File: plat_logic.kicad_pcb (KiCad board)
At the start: 2 copper layers, 100 x 100 mm, 135 parts, among them CN1 GPS_Port, Con2 DS1023-1X2SF11, J1 USB_C_Receptacle, J10 DS1023-1X8SF11, J11 DS1023-1X5SF11, J12 DS1023-1X5SF11, J13 DS1023-1X5SF11, J14 DS1023-1X5SF11, J15 DS1023-1X5SF11, J16 DS1023-1X5SF11, J17 DS1023-1X5SF11, J2 JST_GH_SM06B-GHS-TB, J3 JST_GH_SM06B-GHS-TB, J4 JST_GH_SM06B-GHS-TB, J5 JST_GH_SM06B-GHS-TB, J6 DS1023-1X11S21, J7 DS1023-1X11S21, J8 DS1023-1X6SF11, J9 DS1023-1X11S21, SW1 Button-SMD-4.5x4.5x5.5, SW2 Button-SMD-4.5x4.5x5.5, U1 STM32F429ZITx, U2 USBLC6-2SC6, U3 SN65HVD232, Y1 CSTNE8M00GH5L000R0 8.000MHZ, Y2 NX3215SA-32.768KHZ-EXS00A-MU0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, con1 DS1023-1X3SF11

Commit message: trassing
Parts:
- moved C6 16.5 mm to (127.6, 114.5), turned to 45 degrees
- moved C7 16.3 mm to (129.3, 116.2), turned to -135 degrees
- moved C8 16.3 mm to (130.8, 117.7)
- moved R14 16.3 mm to (131.4, 113.8)
- moved R13 16.3 mm to (130.0, 112.4)
- moved R15 16.2 mm to (132.9, 115.2)
- moved C12 7.85 mm to (134.2, 117.5), turned to 135 degrees
- moved R6 6.45 mm to (167.7, 114.2), turned to -45 degrees
- moved R5 5.99 mm to (165.0, 116.7), turned to -45 degrees
- moved C9 5.40 mm to (168.4, 100.1), turned to 45 degrees
- moved R18 4.74 mm to (168.6, 102.4), turned to -135 degrees
- moved R3 3.25 mm to (166.4, 115.3)
- moved C24 2.55 mm to (161.4, 118.9)
- moved C27 2.54 mm to (158.5, 121.8)
- moved C29 2.49 mm to (156.8, 123.4)
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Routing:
- net GND: track 69.2 -> 126.4 mm
- net +3v3: track 324.9 -> 369.9 mm
- net FS4: track 0.00 -> 15.4 mm, vias 0 -> 1
- net DAC: track 0.00 -> 14.3 mm, vias 0 -> 1
- net IN1_M4: track 0.00 -> 13.9 mm, vias 0 -> 1
- net Net-(U1-PF3): track 0.16 -> 13.6 mm
- net IN2_M4: track 0.00 -> 12.5 mm, vias 0 -> 1
- net Net-(U1-PF4): track 0.00 -> 12.1 mm
- net BOOT1: track 0.00 -> 12.1 mm
- net D7: track 0.00 -> 11.4 mm, vias 0 -> 1
- net Net-(U1-PF5): track 0.00 -> 11.1 mm
- net D6: track 0.00 -> 10.5 mm, vias 0 -> 1
- net ENC_A_M6_mk: track 0.00 -> 8.94 mm, vias 0 -> 1
- net D20: track 0.00 -> 8.49 mm, vias 0 -> 1
- net D19: track 0.00 -> 8.01 mm, vias 0 -> 1
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
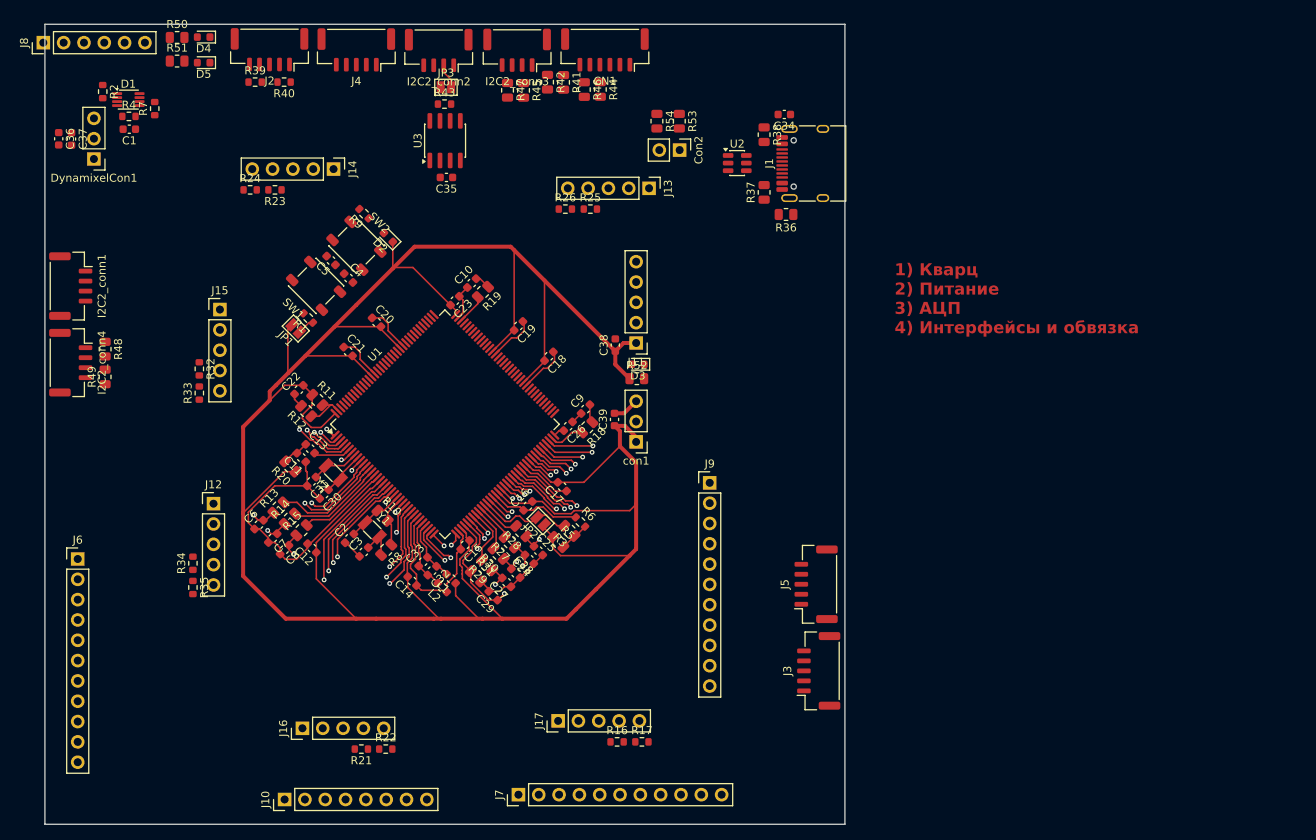
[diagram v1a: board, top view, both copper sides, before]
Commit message: vccTrass
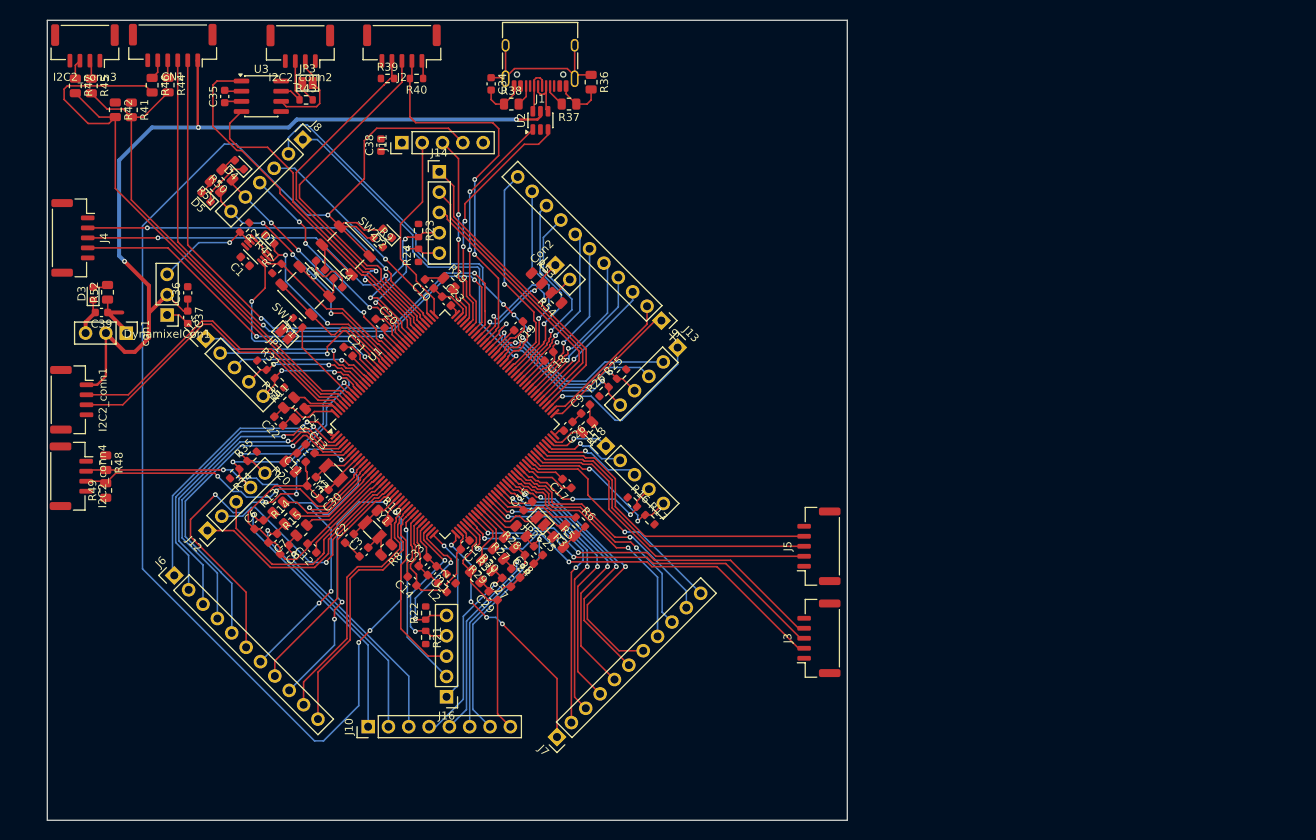
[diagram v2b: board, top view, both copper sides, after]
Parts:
- moved D3 68.7 mm to (106.8, 85.7), turned to 90 degrees
- moved R52 67.0 mm to (108.6, 85.5), turned to 90 degrees
- moved C39 65.5 mm to (107.9, 88.0), turned to 180 degrees
- moved con1 65.2 mm to (111.0, 90.6), turned to -90 degrees
- moved R42 54.1 mm to (109.6, 62.7)
- moved R41 54.1 mm to (111.6, 62.7)
- moved CN1 54.0 mm to (116.8, 54.6)
- moved R45 54.0 mm to (106.6, 59.7)
- moved R47 54.0 mm to (104.6, 59.7)
- moved I2C2_conn3 54.0 mm to (105.8, 54.7)
- moved R44 54.0 mm to (116.2, 59.6)
- moved R46 54.0 mm to (114.2, 59.6)
- moved J4 42.5 mm to (104.3, 78.7), turned to -90 degrees
- moved J11 38.5 mm to (145.4, 66.8), turned to 90 degrees
- moved C38 38.5 mm to (142.8, 67.1)
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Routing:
- net +3v3: track 369.9 -> 73.0 mm
- net NRST: track 1.54 -> 183.0 mm, vias 1 -> 4
- net +5v: track 0.00 -> 111.3 mm, vias 0 -> 3
- net I2C1_SDA: track 0.00 -> 75.9 mm
- net USART1_TX: track 0.00 -> 74.8 mm, vias 0 -> 2
- net USART1_RX: track 0.00 -> 74.7 mm, vias 0 -> 2
- net I2C1_SCL: track 0.00 -> 60.0 mm
- net D34: track 0.00 -> 51.5 mm, vias 0 -> 3
- net SDIO_D0: track 0.00 -> 48.8 mm, vias 0 -> 2
- net SPI3_MISO: track 0.00 -> 48.1 mm, vias 0 -> 2
- net SDIO_CMD: track 0.00 -> 48.1 mm, vias 0 -> 2
- net SPI3_SCK: track 0.00 -> 48.0 mm, vias 0 -> 2
- net SPI1_SCK: track 4.03 -> 51.6 mm, vias 1 -> 2
- net D5: track 1.75 -> 47.9 mm, vias 1 -> 4
- net CAN1_TX: track 0.00 -> 45.9 mm
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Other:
- board text removed: "1) Кварц 2) Питание 3) АЦП 4) Интерфейсы и обвязка"

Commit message: Done
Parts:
- moved D3 75.2 mm to (181.2, 74.8), turned to -90 degrees
- moved C39 73.9 mm to (180.2, 72.5), turned to 0 degrees
- moved R52 71.5 mm to (179.4, 75.0), turned to -90 degrees
- moved con1 69.3 mm to (177.1, 69.9), turned to 90 degrees
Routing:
- net +3v3: track 73.0 -> 887.7 mm, vias 0 -> 38
- net GND: track 157.4 -> 903.5 mm, vias 1 -> 50
- net +5v: track 111.3 -> 136.0 mm, vias 3 -> 4
- net Data: track 41.6 -> 48.5 mm
- net IN2_M4: track 29.2 -> 31.5 mm
- net FS5: track 22.9 -> 24.9 mm
- net CAN1_TX: track 45.9 -> 47.6 mm
- net D27: track 20.6 -> 22.1 mm
- net IN1_M2: track 38.8 -> 40.3 mm
- net NRST: track 183.0 -> 184.4 mm
- net IN2_M2: track 35.7 -> 37.1 mm
- net FS2: track 32.9 -> 34.2 mm
- net D26: track 20.5 -> 21.4 mm
- net CLK: track 24.4 -> 25.2 mm
- net TX_EN: track 27.6 -> 28.4 mm
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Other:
- board text added: "+3v3"
- board text added: "+5v"
- board text added: "A"
- board text added: "A0"
- board text added: "A1"
- board text added: "A2"
- board text added: "A3"
- board text added: "A4"
- board text added: "A5"
- board text added: "A6"
- board text added: "B"
- board text added: "CAN_RX"
- board text added: "CAN_TX"
- board text added: "CLK"
- board text added: "D0"
- board text added: "D1"
- board text added: "D10"
- board text added: "D11"
- board text added: "D12"
- board text added: "D13"
- board text added: "D14"
- board text added: "D15"
- board text added: "D16"
- board text added: "D17"
- board text added: "D18"
- board text added: "D19"
- board text added: "D2"
- board text added: "D20"
- board text added: "D21"
- board text added: "D22"
- board text added: "D23"
- board text added: "D24"
- board text added: "D25"
- board text added: "D26"
- board text added: "D27"
- board text added: "D28"
- board text added: "D29"
- board text added: "D3"
- board text added: "D30"
- board text added: "D31"
- board text added: "D32"
- board text added: "D33"
- board text added: "D34"
- board text added: "D35"
- board text added: "D36"
- board text added: "D37"
- board text added: "D38"
- board text added: "D4"
- board text added: "D5"
- board text added: "D6"
- board text added: "D7"
- board text added: "D8"
- board text added: "D9"
- board text added: "DAC"
- board text added: "Data"
- board text added: "FS"
- board text added: "GND"
- board text added: "I2C1_SCL"
- board text added: "I2C1_SDA"
- board text added: "I2C2_SCL"
- board text added: "I2C2_SDA"
- board text added: "IN1"
- board text added: "IN2"
- board text added: "M1"
- board text added: "M2"
- board text added: "M3"
- board text added: "M4"
- board text added: "M5"
- board text added: "M6"
- board text added: "Motor_I2C3_SCL"
- board text added: "Motor_I2C3_SDA"
- board text added: "NRST"
- board text added: "SPI1_MISO"
- board text added: "SPI1_MOSI"
- board text added: "SPI1_SCK"
- board text added: "SPI3_MISO"
- board text added: "SPI3_MOSI"
- board text added: "SPI3_SCK"
- board text added: "SPI4_MISO"
- board text added: "SPI4_MOSI"
- board text added: "SPI4_SCK"
- board text added: "SWDIO"
- board text added: "UART8_RX"
- board text added: "UART8_TX"
- board text added: "USART1_RX"
- board text added: "USART1_TX"

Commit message: final
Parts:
- removed C2, C3: 12pF, Capacitor_SMD:C_0603_1608Metric
- removed Y1: CSTNE8M00GH5L000R0 8.000MHZ, Crystal:Crystal_SMD_3215-2Pin_3.2x1.5mm
- added Y3: CSTNE8M00GH5L000R0 8.000MHZ, Crystal:Resonator_SMD_Murata_CSTxExxV-3Pin_3.0x1.1mm, F.Cu at (141.7, 115.3)
- moved R8 0.11 mm to (143.4, 117.6)
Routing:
- net +3v3: track 887.7 -> 892.2 mm
- net Net-(R8-Pad2): track 4.29 -> 2.22 mm
- net GND: track 903.5 -> 905.5 mm
- net PH0: track 7.33 -> 5.91 mm
- net Net-(U1-VCAP_2): track 4.87 -> 6.27 mm
- net Net-(U1-PDR_ON): track 10.6 -> 11.5 mm
- net IN1_M5: track 22.1 -> 22.9 mm
- net D0: track 34.9 -> 35.6 mm
- net SWDIO: track 24.2 -> 24.8 mm
- net Net-(U1-PA12): track 30.8 -> 31.4 mm
- net Net-(U1-PA11): track 28.9 -> 29.5 mm
- added copper zone on B.Cu, net GND

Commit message: Финал
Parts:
- moved L2 0.41 mm to (150.1, 122.5)
- moved L1 0.40 mm to (151.2, 121.4)
- moved C32 0.29 mm to (148.9, 120.4)
- moved C33 0.27 mm to (147.8, 119.3)
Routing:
- net IN1_M5: track 22.9 -> 24.0 mm
- net GND: track 905.5 -> 906.3 mm

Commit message: Trass
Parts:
- removed C38: 100nF, Capacitor_SMD:C_0603_1608Metric
- removed C39: 1uF, Capacitor_SMD:C_0603_1608Metric
- removed J13, J14, J15, J16, J17: DS1023-1X5SF11, Connector_PinHeader_2.54mm:PinHeader_1x05_P2.54mm_Vertical
- removed Y3: CSTNE8M00GH5L000R0 8.000MHZ, Crystal:Resonator_SMD_Murata_CSTxExxV-3Pin_3.0x1.1mm
- added A1: Arduino_UNO_R2, CastomLibrary:Arduino_UNO_R2, F.Cu at (191.6, 128.2)
- added C2: 100nF, Capacitor_SMD:C_0603_1608Metric, F.Cu at (133.4, 74.4)
- added C3: 100nF, Capacitor_SMD:C_0603_1608Metric, F.Cu at (133.4, 70.1)
- added JP4: Jumper_3_Open, Connector_PinHeader_2.54mm:PinHeader_1x03_P2.54mm_Vertical, F.Cu at (146.4, 125.2)
- added JP5: Jumper_3_Open, Connector_PinHeader_2.54mm:PinHeader_1x03_P2.54mm_Vertical, F.Cu at (146.3, 128.9)
- added MH1: JetBot_AI_Kit_3x18650_Hole_Pattern, JetBot_Mechanics:JetBot_AI_Kit_3x18650_Hole_Pattern, F.Cu at (101.1, 64.9)
- added Y1: CSTNE8M00GH5L000R0 8.000MHZ, Crystal:Resonator_SMD_Murata_CSTxExxV-3Pin_3.0x1.1mm, F.Cu at (141.4, 115.0)
- C11: value 1uF x5r -> 100nF
- C27: value 100nF -> 22pF
- C28: value 100nF -> 12pF
- C29: value 22pF -> 12pF
- C30: value 12pF -> 100nF
- C31: value 12pF -> 1uF
- C32: value 100nF -> 0.01uF
- C33: value 1uF -> 100nF
- C34: value 0.01uF -> C_Polarized_US
- C35: value 100nF -> 0.1uF
- C36: value C_Polarized_US -> 100nF
- C37: value 0.1uF -> 1uF
- C9: value 100nF -> 1uF x5r
- J10: value DS1023-1X8SF11 -> DS1023-1X5SF11; footprint Connector_PinHeader_2.54mm:PinHeader_1x08_P2.54mm_Vertical -> Connector_PinHeader_2.54mm:PinHeader_1x05_P2.54mm_Vertical
- J11, J12: value DS1023-1X5SF11 -> DS1023-2X10S21; footprint Connector_PinHeader_2.54mm:PinHeader_1x05_P2.54mm_Vertical -> Connector_PinHeader_2.54mm:PinHeader_2x10_P2.54mm_Vertical
- J6: value DS1023-1X11S21 -> DS1023-1X8S21; footprint Connector_PinHeader_2.54mm:PinHeader_1x11_P2.54mm_Vertical -> Connector_PinHeader_2.54mm:PinHeader_1x08_P2.54mm_Vertical
- J8: value DS1023-1X6SF11 -> DS1023-1X4S21; footprint Connector_PinHeader_2.54mm:PinHeader_1x06_P2.54mm_Vertical -> Connector_PinHeader_2.54mm:PinHeader_1x04_P2.54mm_Vertical
- J9: value DS1023-1X11S21 -> DS1023-1X4S21; footprint Connector_PinHeader_2.54mm:PinHeader_1x11_P2.54mm_Vertical -> Connector_PinHeader_2.54mm:PinHeader_1x04_P2.54mm_Vertical
- moved C36 84.2 mm to (189.0, 131.8), turned to -90 degrees
- moved J10 65.8 mm to (144.6, 74.1)
- moved C33 63.1 mm to (123.3, 61.1), turned to 90 degrees
- moved J12 63.0 mm to (179.6, 91.7), turned to 0 degrees
- moved C32 61.4 mm to (156.6, 59.5), turned to -90 degrees
- moved C34 58.2 mm to (107.0, 90.1)
- moved R25 56.8 mm to (116.2, 99.0), turned to 90 degrees
- moved R26 54.7 mm to (116.2, 102.1), turned to 90 degrees
- moved R34 53.1 mm to (177.0, 99.6), turned to 90 degrees
- moved R35 50.4 mm to (177.0, 102.6), turned to -90 degrees
- moved con1 48.3 mm to (178.5, 118.2), turned to -90 degrees
- moved R21 46.4 mm to (184.7, 99.7), turned to 90 degrees
- moved R22 42.9 mm to (184.7, 102.7), turned to -90 degrees
- moved C8 41.3 mm to (154.2, 83.8)
- moved C7 41.1 mm to (168.9, 105.5), turned to 135 degrees
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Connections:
- C10 pad 1: GND -> +3v3
- C10 pad 2: Net-(C10-Pad2) -> GND
- C11 pad 1: GND -> Net-(C11-Pad1)
- C11 pad 2: Net-(C11-Pad2) -> Net-(U1-VBAT)
- C12 pad 1: +3v3 -> GND
- C12 pad 2: GND -> +3v3
- C13 pad 1: Net-(C11-Pad2) -> +3v3
- C13 pad 2: Net-(U1-VBAT) -> GND
- C15 pad 1: +3v3 -> GND
- C15 pad 2: GND -> +3v3
- C22 pad 2: +3v3 -> A5
- C23 pad 1: GND -> A6
- C23 pad 2: +3v3 -> GND
- C24 pad 2: A5 -> +3v3
- C25 pad 1: A6 -> GND
- C25 pad 2: GND -> A3
- C26 pad 1: GND -> A4
- C26 pad 2: +3v3 -> GND
- C27 pad 1: GND -> DAC
- C27 pad 2: A3 -> GND
- C28 pad 1: A4 -> PC15
- C29 pad 1: DAC -> PC14
- C30 pad 1: PC15 -> VDDA
- C30 pad 2: GND -> VREF+
- C31 pad 1: PC14 -> VREF+
- C31 pad 2: GND -> VDDA
- C32 pad 1: VDDA -> Net-(J1-SHIELD)
- C32 pad 2: VREF+ -> GND
- C33 pad 1: VREF+ -> +3v3
- C33 pad 2: VDDA -> GND
- C34 pad 1: Net-(J1-SHIELD) -> +5v
- C35 pad 1: +3v3 -> +5v
- C35 pad 2: GND -> Net-(DynamixelCon1-GND)
- C36 pad 1: +5v -> +3v3
- C37 pad 1: +5v -> +3v3
- C37 pad 2: Net-(DynamixelCon1-GND) -> GND
- C4 pad 1: Net-(C4-Pad1) -> GND
- C4 pad 2: GND -> A0
- C5 pad 1: Net-(C5-Pad1) -> A1
- C6 pad 1: GND -> A2
- C6 pad 2: A0 -> GND
- C7 pad 1: A1 -> GND
- C7 pad 2: GND -> Net-(C7-Pad2)
- C8 pad 1: A2 -> GND
- C8 pad 2: GND -> Net-(C8-Pad2)
- C9 pad 2: Net-(C9-Pad2) -> Net-(C11-Pad1)
- J10 pad 1: A0 -> +3v3
- J10 pad 2: A1 -> CLK
- J10 pad 3: A2 -> SWDIO
- J10 pad 4: A3 -> NRST
- J10 pad 5: A4 -> GND
- J11 pad 1: +3v3 -> IN1_M1
- J11 pad 2: CLK -> IN1_M2
- J11 pad 3: SWDIO -> IN2_M1
- J11 pad 4: NRST -> IN2_M2
- J11 pad 5: GND -> FS1
- J12 pad 2: IN2_M4 -> IN1_M5
- J12 pad 3: FS4 -> IN2_M4
- J12 pad 4: ENC_A_M4_mk -> IN2_M5
- J12 pad 5: ENC_B_M4_mk -> FS4
- J7 pad 1: D11 -> D8
- J7 pad 10: D20 -> D15
- J7 pad 11: D21 -> D16
- J7 pad 2: D12 -> DAC
- J7 pad 3: D13 -> A6
- J7 pad 4: D14 -> D9
- J7 pad 5: D15 -> D10
- J7 pad 6: D16 -> D11
- J7 pad 7: D17 -> D12
- J7 pad 8: D18 -> D13
- J7 pad 9: D19 -> D14
- J8 pad 1: D33 -> D29
- J8 pad 2: D34 -> D30
- J8 pad 3: D35 -> D31
- J8 pad 4: D36 -> D32
- J9 pad 1: D22 -> D17
- J9 pad 2: D23 -> D18
- J9 pad 3: D24 -> D19
- J9 pad 4: D25 -> D20
- R18 pad 1: Net-(C9-Pad2) -> Net-(C7-Pad2)
- R19 pad 1: Net-(C10-Pad2) -> Net-(C8-Pad2)
- R20 pad 2: Net-(C11-Pad2) -> Net-(C11-Pad1)
- R50 pad 1: D37 -> D31
- R51 pad 1: D38 -> D32
- SW1 pad 2: Net-(C4-Pad1) -> Net-(C2-Pad1)
- SW2 pad 2: Net-(C5-Pad1) -> Net-(C3-Pad1)
- U1 pad 110: D35 -> D29
- U1 pad 119: D36 -> D30
- U1 pad 12: D6 -> D4
- U1 pad 123: D37 -> D31
- U1 pad 125: D38 -> D32
- U1 pad 18: FS4 -> PWM_ard
- U1 pad 21: D7 -> FS4
- U1 pad 22: D8 -> D5
- U1 pad 26: D9 -> D6
- U1 pad 27: D10 -> D7
- U1 pad 37: D11 -> D8
- U1 pad 4: D3 -> IN1_M1
- U1 pad 49: D12 -> D9
- U1 pad 5: D4 -> IN1_M2
- U1 pad 50: D13 -> D10
- U1 pad 53: D14 -> D11
- U1 pad 54: D15 -> D12
- U1 pad 55: D16 -> D13
- U1 pad 56: D17 -> D14
- U1 pad 57: D18 -> D15
- U1 pad 58: D19 -> UART7_RX
- U1 pad 59: D20 -> UART7_TX
- U1 pad 63: D21 -> D16
- U1 pad 7: D5 -> D3
- U1 pad 73: D22 -> D17
- U1 pad 74: D23 -> SPI2_SCK
- U1 pad 75: IN1_M1 -> SPI2_MISO
- U1 pad 76: IN1_M2 -> SPI2_MOSI
- U1 pad 79: D24 -> D18
- U1 pad 80: D25 -> D19
- U1 pad 81: D26 -> D20
- U1 pad 82: D27 -> D21
- U1 pad 85: D28 -> D22
- U1 pad 86: D29 -> D23
- U1 pad 87: D30 -> D24
- U1 pad 88: D31 -> D25
- U1 pad 89: D32 -> D26
- U1 pad 90: D33 -> D27
- U1 pad 91: D34 -> D28
- U2 pad 1: Net-(U1-PA11) -> Net-(U1-PA12)
- U2 pad 3: Net-(U1-PA12) -> Net-(U1-PA11)
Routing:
- net GND: track 906.3 -> 11.1 mm, vias 50 -> 0
- net +3v3: track 892.5 -> 9.41 mm, vias 38 -> 0
- net NRST: track 184.4 -> 1.61 mm, vias 4 -> 1
- net +5v: track 136.0 -> 0.00 mm, vias 4 -> 0
- net I2C1_SDA: track 75.9 -> 0.00 mm
- net USART1_TX: track 75.1 -> 0.00 mm, vias 2 -> 0
- net USART1_RX: track 75.1 -> 0.00 mm, vias 2 -> 0
- net I2C1_SCL: track 60.0 -> 0.00 mm
- net SPI1_SCK: track 51.6 -> 0.00 mm, vias 2 -> 0
- net D34: track 51.5 -> 0.00 mm, vias 3 -> 0
- net SPI1_MISO: track 48.9 -> 0.00 mm, vias 2 -> 0
- net SDIO_D0: track 48.8 -> 0.00 mm, vias 2 -> 0
- net Data: track 48.5 -> 0.00 mm, vias 3 -> 0
- net SPI3_MISO: track 48.1 -> 0.00 mm, vias 2 -> 0
- net SDIO_CMD: track 48.1 -> 0.00 mm, vias 2 -> 0
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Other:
- board size 100 x 100 mm -> 120 x 100 mm
